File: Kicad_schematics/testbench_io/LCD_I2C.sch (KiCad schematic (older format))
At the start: 1 part

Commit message: added hierarchical sheets
Signed-off-by: Mojitas <47667093+Mojitas@users.noreply.github.com>
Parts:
- removed U?: LCD_backpack, symbol Solarteam:LCD_backpack
- added C1: C_Small, symbol Device:C_Small
- added D7: LED, symbol Device:LED
- added DS1: HY1602E, Display:HY1602E, symbol Display_Character:HY1602E
- added JP1, JP2, JP3: SolderJumper_2_Open, symbol Jumper:SolderJumper_2_Open
- added Q6: 2N3904, Package_TO_SOT_THT:TO-92_Inline, symbol Transistor_BJT:2N3904
- added R13, R14, R15, R16, R17, R18, R19: R_Small, symbol Device:R_Small
- added RV5: R_POT_Small, symbol Device:R_POT_Small
- added U3: PCF8574, symbol Interface_Expansion:PCF8574
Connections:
- net labels added: LED_(+), LED_(-), pot_brightness
- wire segments 4 -> 68

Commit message: Added footprints
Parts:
- added J201: Conn_01x02, symbol Connector_Generic:Conn_01x02
- C201: renamed from C1; value C_Small -> 100n
- D201: renamed from D7; footprint (none) -> LED_THT:LED_D5.0mm
- R201: renamed from R13; value R_Small -> 1k
- R202: renamed from R14; value R_Small -> 10k
- R203: renamed from R15; value R_Small -> 10k
- R204: renamed from R16; value R_Small -> 10k
- R205: renamed from R17; value R_Small -> 4.7
- R206: renamed from R18; value R_Small -> 4.7
- R207: renamed from R19; value R_Small -> 4.7
- RV201: renamed from RV5; value R_POT_Small -> 10k
- U201: renamed from U3; value PCF8574 -> PCF8574AN
- renumbered DS1 to DS201, JP1 to JP201, JP2 to JP202, JP3 to JP203, Q6 to Q201
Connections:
- net labels added: DB4, DB5, DB6, DB7, E, MCU_5V, RS, RW
- net labels removed: VDD_MCU
- wire segments 68 -> 69
- no-connect marks 0 -> 5
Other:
- moved on the sheet: Q201

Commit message: Started with layout
Signed-off-by: Mojitas <47667093+Mojitas@users.noreply.github.com>
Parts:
- removed J201: Conn_01x02, symbol Connector_Generic:Conn_01x02
- added SW1: SW_DIP_x01, Package_DIP:DIP-4_W7.62mm, symbol Switch:SW_DIP_x01
- C201: footprint (none) -> Package_TO_SOT_SMD:TO-252-2
- DS201: footprint Display:HY1602E -> Display:WC1602A
- JP201, JP202, JP203: footprint (none) -> Jumper:SolderJumper-2_P1.3mm_Open_Pad1.0x1.5mm
- Q201: footprint Package_TO_SOT_THT:TO-92_Inline -> Package_TO_SOT_SMD:SOT-23
- R201, R202, R203, R204, R205, R206, R207: footprint (none) -> Resistor_SMD:R_0603_1608Metric
- RV201: footprint (none) -> Potentiometer_THT:Potentiometer_Bourns_3386P_Vertical
- U201: footprint (none) -> Package_DIP:DIP-16_W7.62mm
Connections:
- wire segments 69 -> 70
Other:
- moved on the sheet: Q201
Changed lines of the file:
@@
 F 0 "U201" H 5050 5881 50  0000 C CNN
 F 1 "PCF8574AN" H 5050 5790 50  0000 C CNN
-F 2 "" H 5050 5000 50  0001 C CNN
+F 2 "Package_DIP:DIP-16_W7.62mm" H 5050 5000 50  0001 C CNN
 F 3 "http://www.nxp.com/documents/data_sheet/PCF8574_PCF8574A.pdf" H 5050 5000 50  0001 C CNN
 	1    5050 5000
@@
 F 0 "RV201" H 3900 3500 50  0000 R CNN
 F 1 "10k" V 3550 3650 50  0000 R CNN
-F 2 "" H 3650 3600 50  0001 C CNN
+F 2 "Potentiometer_THT:Potentiometer_Bourns_3386P_Vertical" H 3650 3600 50  0001 C CNN
 F 3 "~" H 3650 3600 50  0001 C CNN
 	1    3650 3600
@@
 F 0 "C201" H 5192 5846 50  0000 L CNN
 F 1 "100n" H 5192 5755 50  0000 L CNN
-F 2 "" H 5100 5800 50  0001 C CNN
+F 2 "Package_TO_SOT_SMD:TO-252-2" H 5100 5800 50  0001 C CNN
 F 3 "~" H 5100 5800 50  0001 C CNN
 	1    5100 5800
@@
 F 0 "JP201" V 2950 5500 50  0000 L CNN
 F 1 "SolderJumper_2_Open" H 2050 5400 50  0000 L CNN
-F 2 "" H 2750 5500 50  0001 C CNN
+F 2 "Jumper:SolderJumper-2_P1.3mm_Open_Pad1.0x1.5mm" H 2750 5500 50  0001 C CNN
 F 3 "~" H 2750 5500 50  0001 C CNN
 	1    2750 5500
@@
 F 0 "R205" H 4059 4246 50  0000 L CNN
 F 1 "4.7" V 3900 4050 50  0000 L CNN
-F 2 "" H 4000 4200 50  0001 C CNN
+F 2 "Resistor_SMD:R_0603_1608Metric" H 4000 4200 50  0001 C CNN
 F 3 "~" H 4000 4200 50  0001 C CNN
 	1    4000 4200
@@
 F 0 "R201" V 2300 4850 50  0000 L CNN
 F 1 "1k" V 2300 4700 50  0000 L CNN
-F 2 "" H 2400 4850 50  0001 C CNN
+F 2 "Resistor_SMD:R_0603_1608Metric" H 2400 4850 50  0001 C CNN
 F 3 "~" H 2400 4850 50  0001 C CNN
 	1    2400 4850
@@
 F 0 "R203" H 3109 4246 50  0000 L CNN
 F 1 "10k" V 2950 4050 50  0000 L CNN
-F 2 "" H 3050 4200 50  0001 C CNN
+F 2 "Resistor_SMD:R_0603_1608Metric" H 3050 4200 50  0001 C CNN
 F 3 "~" H 3050 4200 50  0001 C CNN
 	1    3050 4200
@@
 F 0 "R202" H 2809 4246 50  0000 L CNN
 F 1 "10k" V 2650 4050 50  0000 L CNN
-F 2 "" H 2750 4200 50  0001 C CNN
+F 2 "Resistor_SMD:R_0603_1608Metric" H 2750 4200 50  0001 C CNN
 F 3 "~" H 2750 4200 50  0001 C CNN
 	1    2750 4200
@@
 F 0 "R206" H 4359 4246 50  0000 L CNN
 F 1 "4.7" V 4200 4050 50  0000 L CNN
-F 2 "" H 4300 4200 50  0001 C CNN
+F 2 "Resistor_SMD:R_0603_1608Metric" H 4300 4200 50  0001 C CNN
 F 3 "~" H 4300 4200 50  0001 C CNN
 	1    4300 4200
@@
 F 0 "JP202" V 3250 5500 50  0000 L CNN
 F 1 "SolderJumper_2_Open" H 2400 5400 50  0000 L CNN
-F 2 "" H 3050 5500 50  0001 C CNN
+F 2 "Jumper:SolderJumper-2_P1.3mm_Open_Pad1.0x1.5mm" H 3050 5500 50  0001 C CNN
 F 3 "~" H 3050 5500 50  0001 C CNN
 	1    3050 5500
@@
 F 0 "JP203" V 3550 5500 50  0000 L CNN
 F 1 "SolderJumper_2_Open" H 2650 5400 50  0000 L CNN
-F 2 "" H 3350 5500 50  0001 C CNN
+F 2 "Jumper:SolderJumper-2_P1.3mm_Open_Pad1.0x1.5mm" H 3350 5500 50  0001 C CNN
 F 3 "~" H 3350 5500 50  0001 C CNN
 	1    3350 5500
@@
 	5100 6050 5100 5900
 $Comp
-L Transistor_BJT:2N3904 Q201
-U 1 1 60006EA0
-P 6700 3100
-F 0 "Q201" H 6890 3146 50  0000 L CNN
-F 1 "2N3904" H 6890 3055 50  0000 L CNN
-F 2 "Package_TO_SOT_THT:TO-92_Inline" H 6900 3025 50  0001 L CIN
-F 3 "https://www.onsemi.com/pub/Collateral/2N3903-D.PDF" H 6700 3100 50  0001 L CNN
-	1    6700 3100
-	1    0    0    -1
-$EndComp
-$Comp
 L Device:R_Small R207
 U 1 1 60007DA4
@@
 F 0 "R207" H 6209 4096 50  0000 L CNN
 F 1 "4.7" V 6050 3900 50  0000 L CNN
-F 2 "" H 6150 4050 50  0001 C CNN
+F 2 "Resistor_SMD:R_0603_1608Metric" H 6150 4050 50  0001 C CNN
 F 3 "~" H 6150 4050 50  0001 C CNN
 	1    6150 4050
@@
 L Display_Character:HY1602E DS201
 U 1 1 60052C13
-P 7750 4700
-F 0 "DS201" H 7750 5681 50  0000 C CNN
-F 1 "HY1602E" H 7750 5590 50  0000 C CNN
-F 2 "Display:HY1602E" H 7750 3800 50  0001 C CIN
-F 3 "http://www.icbank.com/data/ICBShop/board/HY1602E.pdf" H 7950 4800 50  0001 C CNN
-	1    7750 4700
-	1    0    0    -1
-$EndComp
-Text Label 8300 4100 0    50   ~ 0
+P 8500 4750
+F 0 "DS201" H 8500 5731 50  0000 C CNN
+F 1 "HY1602E" H 8500 5640 50  0000 C CNN
+F 2 "Display:WC1602A" H 8500 3850 50  0001 C CIN
+F 3 "http://www.icbank.com/data/ICBShop/board/HY1602E.pdf" H 8700 4850 50  0001 C CNN
+	1    8500 4750
+	1    0    0    -1
+$EndComp
+Text Label 9050 4150 0    50   ~ 0
 pot_brightness
 Wire Wire Line
-	8300 4100 8150 4100
+	9050 4150 8900 4150
 Text Label 3950 3600 0    50   ~ 0
 pot_brightness
 Wire Wire Line
 	3950 3600 3750 3600
-Wire Wire Line
-	6800 2750 6800 2900
-Text Label 8300 4800 0    50   ~ 0
+Text Label 9050 4850 0    50   ~ 0
 LED_(-)
 Wire Wire Line
-	8300 4800 8150 4800
-Text Label 8300 4700 0    50   ~ 0
+	9050 4850 8900 4850
+Text Label 9050 4750 0    50   ~ 0
 LED_(+)
 Wire Wire Line
-	8300 4700 8150 4700
+	9050 4750 8900 4750
 Wire Wire Line
 	2400 3900 2650 3900
@@
 Wire Wire Line
 	3650 3900 4000 3900
-Text GLabel 7750 5700 2    50   Input ~ 0
+Text GLabel 8500 5750 2    50   Input ~ 0
 GND_MCU
 Wire Wire Line
-	7750 5700 7750 5500
+	8500 5750 8500 5550
 NoConn ~ 4550 5400
-NoConn ~ 7350 4600
-NoConn ~ 7350 4700
-NoConn ~ 7350 4800
-NoConn ~ 7350 4900
-Wire Wire Line
-	7950 3900 7750 3900
-Text Label 6800 2750 0    50   ~ 0
-LED_(-)
-Wire Wire Line
-	6150 4200 6500 4200
-Text GLabel 6800 3450 2    50   Input ~ 0
-GND_MCU
-Wire Wire Line
-	6800 3450 6800 3300
-Text Label 7850 2950 2    50   ~ 0
+NoConn ~ 8100 4650
+NoConn ~ 8100 4750
+NoConn ~ 8100 4850
+NoConn ~ 8100 4950
+Wire Wire Line
+	8700 3950 8500 3950
+Text Label 8900 3400 0    50   ~ 0
 LED_(+)
 Text GLabel 2400 3900 1    50   Input ~ 0
@@
 Text GLabel 5100 6050 2    50   Input ~ 0
 MCU_5V
-Text GLabel 7950 3900 2    50   Input ~ 0
+Text GLabel 8700 3950 2    50   Input ~ 0
 MCU_5V
 $Comp
@@
 Wire Wire Line
 	2650 3900 2750 3900
-$Comp
-L Connector_Generic:Conn_01x02 J201
-U 1 1 603F5B07
-P 8050 2950
-F 0 "J201" H 8130 2942 50  0000 L CNN
-F 1 "Conn_01x02" H 8130 2851 50  0000 L CNN
-F 2 "" H 8050 2950 50  0001 C CNN
-F 3 "~" H 8050 2950 50  0001 C CNN
-	1    8050 2950
-	1    0    0    -1
-$EndComp
-Text GLabel 7850 3050 0    50   Input ~ 0
+Text GLabel 8100 3400 0    50   Input ~ 0
 MCU_5V
-Wire Wire Line
-	6500 3100 6500 4200
-Text Label 7250 4400 2    50   ~ 0
+Text Label 8000 4450 2    50   ~ 0
 RS
 Wire Wire Line
-	7250 4400 7350 4400
+	8000 4450 8100 4450
 Text Label 5650 4600 0    50   ~ 0
 RS
 Wire Wire Line
 	5650 4600 5550 4600
-Text Label 7250 4300 2    50   ~ 0
+Text Label 8000 4350 2    50   ~ 0
 RW
 Wire Wire Line
-	7250 4300 7350 4300
+	8000 4350 8100 4350
 Text Label 5650 4700 0    50   ~ 0
 RW
 Wire Wire Line
 	5650 4700 5550 4700
-Text Label 7250 4100 2    50   ~ 0
+Text Label 8000 4150 2    50   ~ 0
 E
 Wire Wire Line
-	7250 4100 7350 4100
+	8000 4150 8100 4150
 Text Label 5650 4800 0    50   ~ 0
 E
@@
 Wire Wire Line
 	5550 5300 5650 5300
-Text Label 7250 5000 2    50   ~ 0
+Text Label 8000 5050 2    50   ~ 0
 DB4
-Text Label 7250 5100 2    50   ~ 0
+Text Label 8000 5150 2    50   ~ 0
 DB5
-Text Label 7250 5200 2    50   ~ 0
+Text Label 8000 5250 2    50   ~ 0
 DB6
-Text Label 7250 5300 2    50   ~ 0
+Text Label 8000 5350 2    50   ~ 0
 DB7
 Wire Wire Line
-	7250 5000 7350 5000
-Wire Wire Line
-	7250 5100 7350 5100
-Wire Wire Line
-	7250 5200 7350 5200
-Wire Wire Line
-	7250 5300 7350 5300
+	8000 5050 8100 5050
+Wire Wire Line
+	8000 5150 8100 5150
+Wire Wire Line
+	8000 5250 8100 5250
+Wire Wire Line
+	8000 5350 8100 5350
 $Comp
 L Device:R_Small R204
@@
 F 0 "R204" H 3409 4246 50  0000 L CNN
 F 1 "10k" V 3250 4050 50  0000 L CNN
-F 2 "" H 3350 4200 50  0001 C CNN
+F 2 "Resistor_SMD:R_0603_1608Metric" H 3350 4200 50  0001 C CNN
 F 3 "~" H 3350 4200 50  0001 C CNN
 	1    3350 4200
 	1    0    0    -1
 $EndComp
+$Comp
+L Switch:SW_DIP_x01 SW1
+U 1 1 600B20D2
+P 8500 3400
+F 0 "SW1" H 8500 3667 50  0000 C CNN
+F 1 "SW_DIP_x01" H 8500 3576 50  0000 C CNN
+F 2 "Package_DIP:DIP-4_W7.62mm" H 8500 3400 50  0001 C CNN
+F 3 "~" H 8500 3400 50  0001 C CNN
+	1    8500 3400
+	1    0    0    -1
+$EndComp
+Wire Wire Line
+	8200 3400 8100 3400
+Wire Wire Line
+	8900 3400 8800 3400
+Wire Wire Line
+	6150 4200 6500 4200
+Wire Wire Line
+	6800 4550 6800 4400
+Text GLabel 6800 4550 2    50   Input ~ 0
+GND_MCU
+Text Label 6800 3850 0    50   ~ 0
+LED_(-)
+Wire Wire Line
+	6800 3850 6800 4000
+$Comp
+L Transistor_BJT:2N3904 Q201
+U 1 1 60006EA0
+P 6700 4200
+F 0 "Q201" H 6890 4246 50  0000 L CNN
+F 1 "2N3904" H 6890 4155 50  0000 L CNN
+F 2 "Package_TO_SOT_SMD:SOT-23" H 6900 4125 50  0001 L CIN
+F 3 "https://www.onsemi.com/pub/Collateral/2N3903-D.PDF" H 6700 4200 50  0001 L CNN
+	1    6700 4200
+	1    0    0    -1
+$EndComp

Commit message: Pcb-layout is on the way
Signed-off-by: Mojitas <47667093+Mojitas@users.noreply.github.com>
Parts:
- removed DS201: HY1602E, Display:WC1602A, symbol Display_Character:HY1602E
- added DS201: WC1602A, Display:WC1602A, symbol Display_Character:WC1602A
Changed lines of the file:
@@
 Wire Wire Line
 	6150 4200 6150 4900
-$Comp
-L Display_Character:HY1602E DS201
-U 1 1 60052C13
-P 8500 4750
-F 0 "DS201" H 8500 5731 50  0000 C CNN
-F 1 "HY1602E" H 8500 5640 50  0000 C CNN
-F 2 "Display:WC1602A" H 8500 3850 50  0001 C CIN
-F 3 "http://www.icbank.com/data/ICBShop/board/HY1602E.pdf" H 8700 4850 50  0001 C CNN
-	1    8500 4750
-	1    0    0    -1
-$EndComp
 Text Label 9050 4150 0    50   ~ 0
 pot_brightness
@@
 Wire Wire Line
 	3950 3600 3750 3600
-Text Label 9050 4850 0    50   ~ 0
+Text Label 9050 4550 0    50   ~ 0
 LED_(-)
 Wire Wire Line
-	9050 4850 8900 4850
-Text Label 9050 4750 0    50   ~ 0
+	9050 4550 8900 4550
+Text Label 9050 4450 0    50   ~ 0
 LED_(+)
 Wire Wire Line
-	9050 4750 8900 4750
+	9050 4450 8900 4450
 Wire Wire Line
 	2400 3900 2650 3900
@@
 Wire Wire Line
 	8700 3950 8500 3950
-Text Label 8900 3400 0    50   ~ 0
+Text Label 9050 3400 0    50   ~ 0
 LED_(+)
 Text GLabel 2400 3900 1    50   Input ~ 0
@@
 Text GLabel 8100 3400 0    50   Input ~ 0
 MCU_5V
-Text Label 8000 4450 2    50   ~ 0
+Text Label 8000 4350 2    50   ~ 0
 RS
 Wire Wire Line
-	8000 4450 8100 4450
+	8000 4350 8100 4350
 Text Label 5650 4600 0    50   ~ 0
 RS
 Wire Wire Line
 	5650 4600 5550 4600
-Text Label 8000 4350 2    50   ~ 0
+Text Label 8000 4250 2    50   ~ 0
 RW
 Wire Wire Line
-	8000 4350 8100 4350
+	8000 4250 8100 4250
 Text Label 5650 4700 0    50   ~ 0
 RW
@@
 	8200 3400 8100 3400
 Wire Wire Line
-	8900 3400 8800 3400
-Wire Wire Line
 	6150 4200 6500 4200
-Wire Wire Line
-	6800 4550 6800 4400
 Text GLabel 6800 4550 2    50   Input ~ 0
 GND_MCU
@@
 	1    0    0    -1
 $EndComp
+$Comp
+L Display_Character:WC1602A DS201
+U 1 1 6007F52E
+P 8500 4750
+F 0 "DS201" H 8500 5731 50  0000 C CNN
+F 1 "WC1602A" H 8500 5640 50  0000 C CNN
+F 2 "Display:WC1602A" H 8500 3850 50  0001 C CIN
+F 3 "http://www.wincomlcd.com/pdf/WC1602A-SFYLYHTC06.pdf" H 9200 4750 50  0001 C CNN
+	1    8500 4750
+	1    0    0    -1
+$EndComp
+Wire Wire Line
+	6800 4400 6800 4550
+Wire Wire Line
+	8800 3400 9050 3400
 $EndSCHEMATC

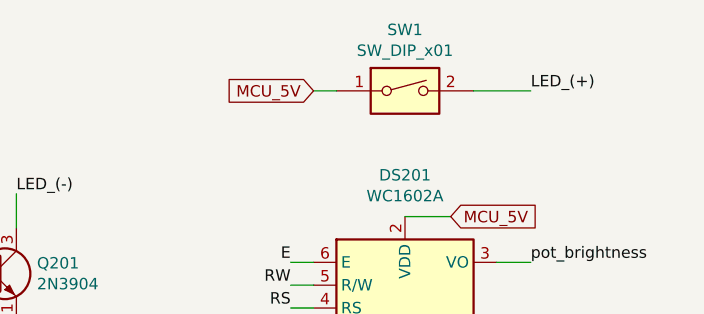
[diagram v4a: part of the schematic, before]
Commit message: Routing done and power planes added
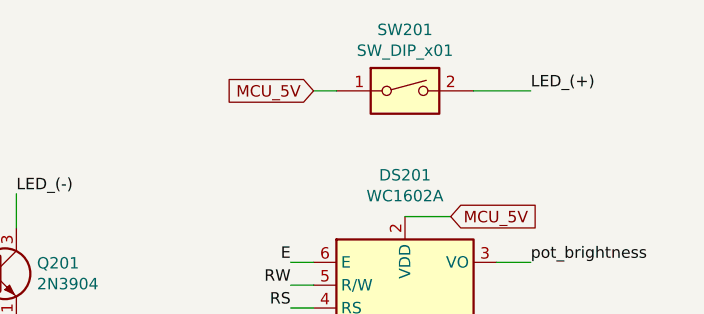
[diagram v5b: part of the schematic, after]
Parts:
- C201: footprint Package_TO_SOT_SMD:TO-252-2 -> Capacitor_SMD:C_0805_2012Metric
- renumbered SW1 to SW201
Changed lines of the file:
@@
 F 0 "C201" H 5192 5846 50  0000 L CNN
 F 1 "100n" H 5192 5755 50  0000 L CNN
-F 2 "Package_TO_SOT_SMD:TO-252-2" H 5100 5800 50  0001 C CNN
+F 2 "Capacitor_SMD:C_0805_2012Metric" H 5100 5800 50  0001 C CNN
 F 3 "~" H 5100 5800 50  0001 C CNN
 	1    5100 5800
@@
 MCU_5V
 $Comp
-L power:PWR_FLAG #FLG0103
+L power:PWR_FLAG #FLG0201
 U 1 1 603F18A6
 P 2650 3900
-F 0 "#FLG0103" H 2650 3975 50  0001 C CNN
+F 0 "#FLG0201" H 2650 3975 50  0001 C CNN
 F 1 "PWR_FLAG" H 2650 4073 50  0000 C CNN
 F 2 "" H 2650 3900 50  0001 C CNN
@@
 $EndComp
 $Comp
-L Switch:SW_DIP_x01 SW1
+L Switch:SW_DIP_x01 SW201
 U 1 1 600B20D2
 P 8500 3400
-F 0 "SW1" H 8500 3667 50  0000 C CNN
+F 0 "SW201" H 8500 3667 50  0000 C CNN
 F 1 "SW_DIP_x01" H 8500 3576 50  0000 C CNN
 F 2 "Package_DIP:DIP-4_W7.62mm" H 8500 3400 50  0001 C CNN

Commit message: fixes
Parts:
- SW201: footprint Package_DIP:DIP-4_W7.62mm -> Package_DIP:Vishay_HVM-DIP-3_W7.62mm
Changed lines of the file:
@@
 F 0 "SW201" H 8500 3667 50  0000 C CNN
 F 1 "SW_DIP_x01" H 8500 3576 50  0000 C CNN
-F 2 "Package_DIP:DIP-4_W7.62mm" H 8500 3400 50  0001 C CNN
+F 2 "Package_DIP:Vishay_HVM-DIP-3_W7.62mm" H 8500 3400 50  0001 C CNN
 F 3 "~" H 8500 3400 50  0001 C CNN
 	1    8500 3400

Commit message: Updated CAN sheet to ethernet interface
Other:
- note added: "I2C address jumpers\n"
- note added: "IO-expander\n"
- note added: "LCD"
- note added: "Manual backlight switch"
- note added: "Signal transistor for backlight"
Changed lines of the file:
@@
 Wire Wire Line
 	8800 3400 9050 3400
+Text Notes 6350 3700 0    50   ~ 0
+Signal transistor for backlight
+Text Notes 8950 5200 0    50   ~ 0
+LCD
+Text Notes 5600 5550 0    50   ~ 0
+IO-expander\n
+Text Notes 2800 6050 0    50   ~ 0
+I2C address jumpers\n
+Text Notes 8000 3000 0    50   ~ 0
+Manual backlight switch
 $EndSCHEMATC
